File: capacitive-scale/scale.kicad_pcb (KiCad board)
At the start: 2 copper layers, 47.3 x 206 mm, 6 parts, among them J101 TEST_1P, J102 TEST_1P, J103 TEST_1P, J104 TEST_1P, U101 outline, U102 scales

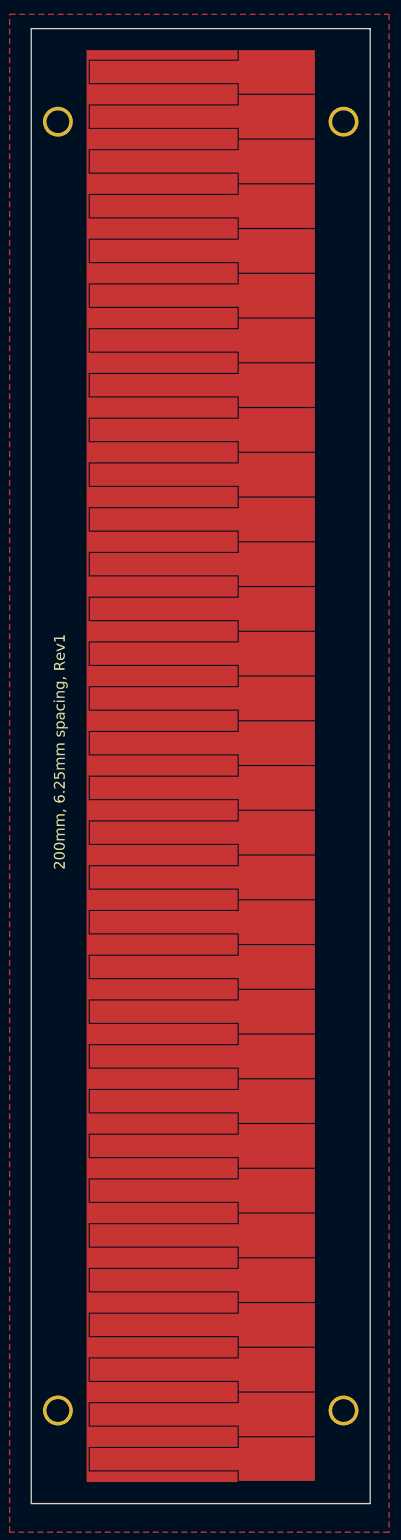
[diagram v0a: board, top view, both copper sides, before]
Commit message: Relayout capacitive scale and regenerate all Gerber files
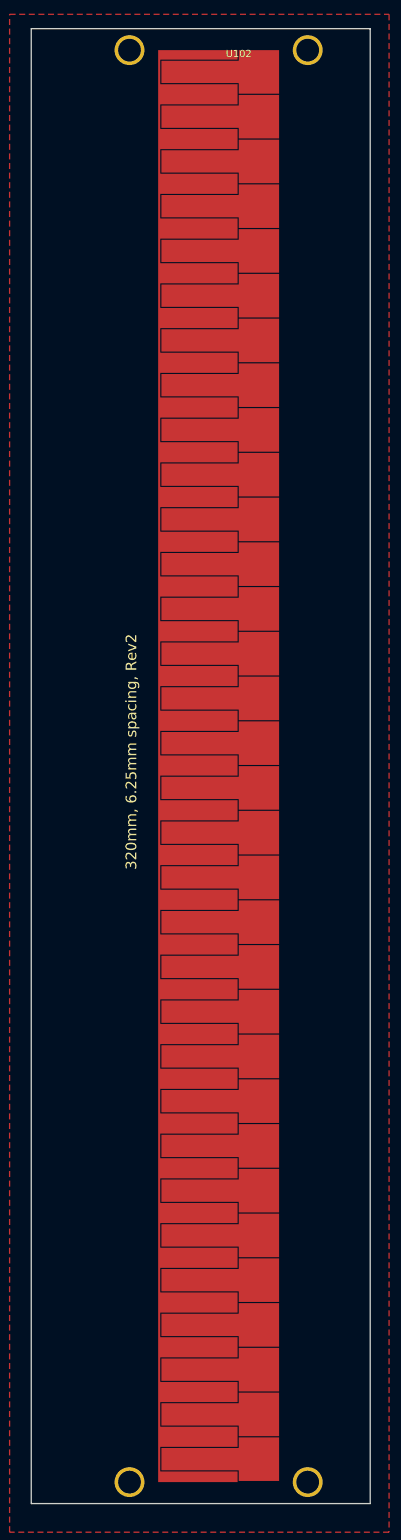
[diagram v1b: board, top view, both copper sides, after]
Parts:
- moved J101 10.0 mm to (100.0, 100.0)
- moved J102 10.0 mm to (100.0, 100.0)
- moved J103 10.0 mm to (100.0, 300.0)
- moved J104 10.0 mm to (100.0, 300.0)
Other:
- board text added: "320mm, 6.25mm spacing, Rev2"
- board text removed: "200mm, 6.25mm spacing, Rev1"

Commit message: Relayout capacitive scale and regenerate all Gerber files
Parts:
- U102: footprint capacitive:Capacitive_Scales200.00 -> capacitive:Capacitive_Scales320.00
- moved U101 100.0 mm to (100.0, 0.00)
- moved U102 100.0 mm to (100.0, 0.00)
- moved J101 90.0 mm to (100.0, 10.0)
- moved J102 90.0 mm to (100.0, 10.0)
- moved J103 10.0 mm to (100.0, 310.0)
- moved J104 10.0 mm to (100.0, 310.0)
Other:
- board size 47.3 x 206 mm -> 32.4 x 321 mm
- board text added: "320mm, 6.25mm spacing Rev2"
- board text removed: "320mm, 6.25mm spacing, Rev2"
